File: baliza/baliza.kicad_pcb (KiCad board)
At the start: 2 copper layers, 76.2 x 66 mm, 27 parts, among them J1 ALIMENTACION, J2 PTT, J3 AUDIO, J4 VCC_13v8_ENTRADA, K1 SRD-05VDC-SL-C, K2 SRD-05VDC-SL-C, Q1 2N3904, Q2 2N3904, U1 L7805

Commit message: actualizacion
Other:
- board text added: "+5V OUT"
- board text added: "13v8 ENTRADA"
- board text added: "7805"
- board text added: "ALIMENTACION"
- board text added: "APAGADO 1"
- board text added: "APAGADO 2"
- board text added: "APAGADO 3"
- board text added: "AUDIO"
- board text added: "GND"
- board text added: "PTT"
- board text added: "RESET"
- board text added: "VCC INPUT"
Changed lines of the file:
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@@
     (property "Sheetname" "")
     (attr through_hole)
-    (fp_text reference "K1" (at 8.1 9.2) (layer "F.SilkS")
+    (fp_text reference "K1" (at 14.4 -8.89) (layer "F.SilkS")
       (effects (font (size 1 1) (thickness 0.15)))
     )
@@
     (property "Sheetname" "")
     (attr through_hole)
-    (fp_text reference "C2" (at 2.5 -2.5) (layer "F.SilkS")
+    (fp_text reference "C2" (at 7.58 0) (layer "F.SilkS")
       (effects (font (size 1 1) (thickness 0.15)))
     )
@@
     (property "Sheetname" "")
     (attr through_hole)
-    (fp_text reference "D1" (at 5.08 -2.47 90) (layer "F.SilkS")
+    (fp_text reference "D1" (at -2.54 0 90) (layer "F.SilkS")
       (effects (font (size 1 1) (thickness 0.15)))
     )
@@
     (property "Sheetname" "")
     (attr through_hole)
-    (fp_text reference "D2" (at 5.08 -2.47 90) (layer "F.SilkS")
+    (fp_text reference "D2" (at -2.54 0 90) (layer "F.SilkS")
       (effects (font (size 1 1) (thickness 0.15)))
     )
@@
     (property "Sheetname" "")
     (attr through_hole)
-    (fp_text reference "J1" (at 2.5 -6.06) (layer "F.SilkS")
+    (fp_text reference "J1" (at -5.08 3.175) (layer "F.SilkS")
       (effects (font (size 1 1) (thickness 0.15)))
     )
@@
     (property "Sheetname" "")
     (attr exclude_from_pos_files)
-    (fp_text reference "JP4" (at 0 -1.8 90) (layer "F.SilkS")
+    (fp_text reference "JP4" (at 0 -3.175 180) (layer "F.SilkS")
       (effects (font (size 1 1) (thickness 0.15)))
     )
@@
   (gr_line (start 88.9 53.34) (end 162.56 53.34) (layer "Edge.Cuts") (width 0.1))
   (gr_line (start 165.1 119.38) (end 88.9 119.38) (layer "Edge.Cuts") (width 0.1))
+  (gr_text "VCC INPUT" (at 133.35 58.42 90) (layer "F.SilkS")
+    (effects (font (size 1 1) (thickness 0.15)))
+  )
+  (gr_text "GND" (at 138.43 115.57) (layer "F.SilkS")
+    (effects (font (size 1 1) (thickness 0.15)))
+  )
+  (gr_text "13v8 ENTRADA" (at 99.06 66.675) (layer "F.SilkS")
+    (effects (font (size 1 1) (thickness 0.15)))
+  )
+  (gr_text "GND" (at 106.68 58.42 90) (layer "F.SilkS")
+    (effects (font (size 1 1) (thickness 0.15)))
+  )
+  (gr_text "PTT" (at 100.33 107.315) (layer "F.SilkS")
+    (effects (font (size 1 1) (thickness 0.15)))
+  )
   (gr_text "BALIZA EA7HG-F4LEC" (at 162.56 93.98 90) (layer "F.SilkS")
     (effects (font (size 2 2) (thickness 0.15)))
   )
+  (gr_text "APAGADO 2" (at 129.54 104.14 90) (layer "F.SilkS")
+    (effects (font (size 1 1) (thickness 0.15)))
+  )
+  (gr_text "RESET" (at 133.35 72.39) (layer "F.SilkS")
+    (effects (font (size 1 1) (thickness 0.15)))
+  )
+  (gr_text "VCC INPUT" (at 114.3 63.5 90) (layer "F.SilkS")
+    (effects (font (size 1 1) (thickness 0.15)))
+  )
+  (gr_text "7805" (at 120.65 58.42) (layer "F.SilkS")
+    (effects (font (size 1 1) (thickness 0.15)))
+  )
+  (gr_text "+5V OUT" (at 127 64.135 90) (layer "F.SilkS")
+    (effects (font (size 1 1) (thickness 0.15)))
+  )
+  (gr_text "ALIMENTACION\n" (at 139.7 64.77) (layer "F.SilkS")
+    (effects (font (size 1 1) (thickness 0.15)))
+  )
+  (gr_text "GND" (at 105.41 108.585) (layer "F.SilkS")
+    (effects (font (size 1 1) (thickness 0.15)))
+  )
+  (gr_text "AUDIO" (at 111.76 107.315) (layer "F.SilkS")
+    (effects (font (size 1 1) (thickness 0.15)))
+  )
+  (gr_text "APAGADO 1" (at 124.46 104.14 90) (layer "F.SilkS")
+    (effects (font (size 1 1) (thickness 0.15)))
+  )
+  (gr_text "APAGADO  3" (at 134.62 104.14 90) (layer "F.SilkS")
+    (effects (font (size 1 1) (thickness 0.15)))
+  )
+  (gr_text "GND" (at 146.05 58.42 90) (layer "F.SilkS")
+    (effects (font (size 1 1) (thickness 0.15)))
+  )
   (segment (start 139.7 74.93) (end 133.35 74.93) (width 1) (layer "F.Cu") (net 3))

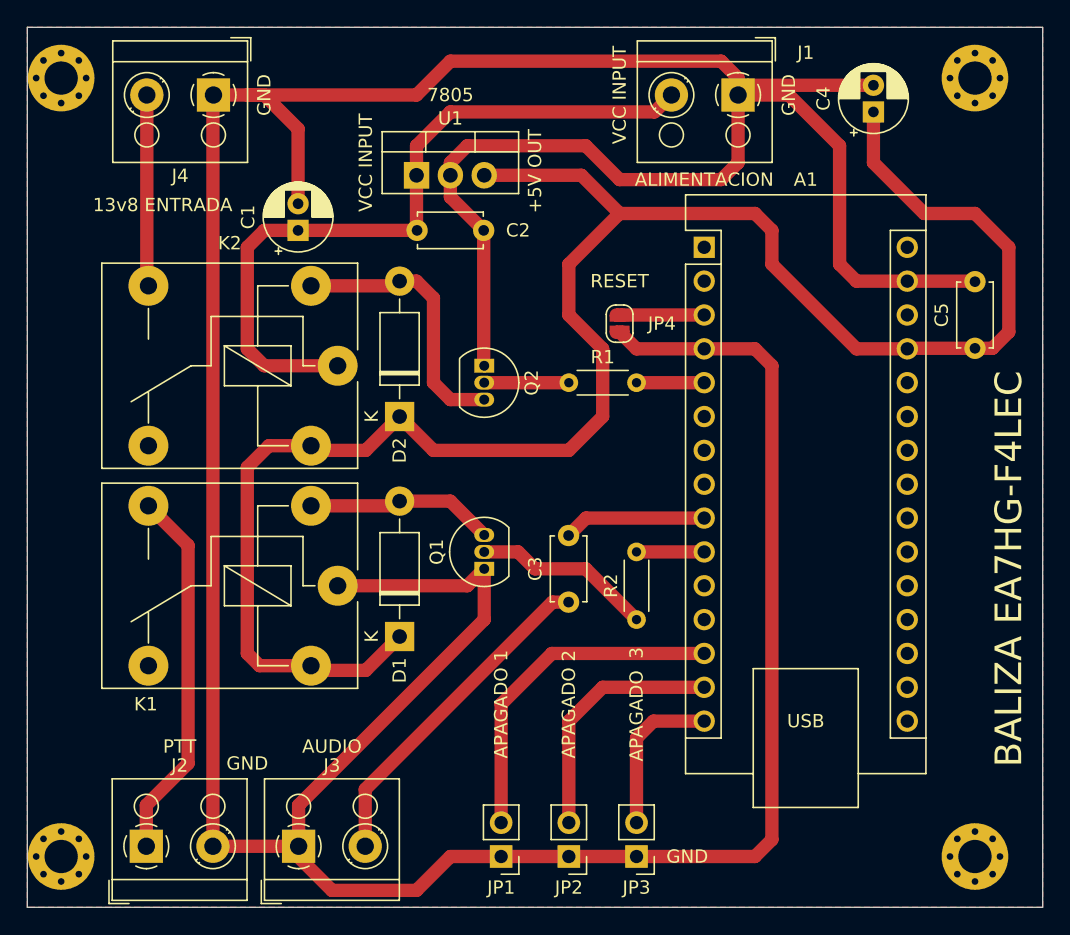
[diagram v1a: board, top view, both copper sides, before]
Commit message: anadir LEDs auxiliares, pistas en cara inferior
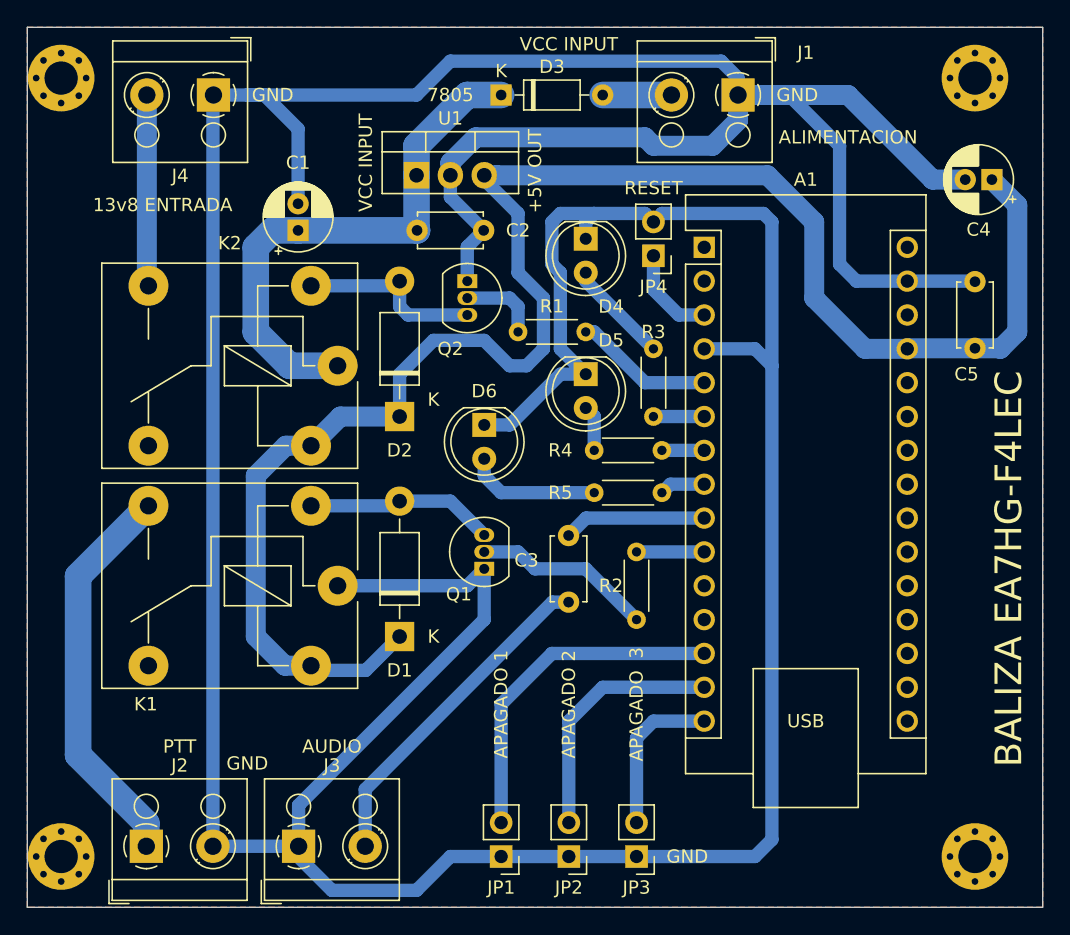
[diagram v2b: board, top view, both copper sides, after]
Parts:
- added D3: 1N4148, Diode_THT:D_DO-35_SOD27_P7.62mm_Horizontal, F.Cu at (124.5, 58.4)
- added D4: LED, LED_THT:LED_D5.0mm, F.Cu at (130.8, 69.2)
- added D5: LED, LED_THT:LED_D5.0mm, F.Cu at (130.8, 79.4)
- added D6: LED, LED_THT:LED_D5.0mm, F.Cu at (123.2, 83.2)
- added R3: 680, Resistor_THT:R_Axial_DIN0204_L3.6mm_D1.6mm_P5.08mm_Horizontal, F.Cu at (135.9, 82.5)
- added R4: 680, Resistor_THT:R_Axial_DIN0204_L3.6mm_D1.6mm_P5.08mm_Horizontal, F.Cu at (136.5, 85.1)
- added R5: 680, Resistor_THT:R_Axial_DIN0204_L3.6mm_D1.6mm_P5.08mm_Horizontal, F.Cu at (136.5, 88.3)
- JP4: footprint Jumper:SolderJumper-2_P1.3mm_Open_RoundedPad1.0x1.5mm -> Connector_PinHeader_2.54mm:PinHeader_1x02_P2.54mm_Vertical
- moved C4 10.2 mm to (161.3, 64.8), turned to 180 degrees
- moved Q2 6.48 mm to (121.9, 72.4)
- moved JP4 5.69 mm to (135.9, 70.5), turned to 180 degrees
- moved R1 5.39 mm to (125.7, 76.2)
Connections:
- A1 pad 6: unconnected-(A1-Pad6) -> AUX1
- A1 pad 7: unconnected-(A1-Pad7) -> AUX2
- A1 pad 8: unconnected-(A1-Pad8) -> AUX3
- J1 pad 2: VCC -> +BATT
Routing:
- net GND: track 324.9 -> 371.2 mm
- net VCC: track 55.3 -> 40.5 mm
- net +5V: track 145.2 -> 130.8 mm
- net Net-(D6-Pad2): track 0.00 -> 10.1 mm
- net Net-(D4-Pad2): track 0.00 -> 7.82 mm
- net Net-(D2-Pad2): track 20.5 -> 14.0 mm
- net /Rele encendido: track 5.08 -> 10.5 mm
- net +BATT: track 0.00 -> 5.16 mm
- net AUX1: track 0.00 -> 3.81 mm
- net Net-(D5-Pad2): track 0.00 -> 3.44 mm
- net AUX3: track 0.00 -> 3.44 mm
- net AUX2: track 0.00 -> 3.17 mm
- net PTT_TRANSCEPTOR: track 28.1 -> 29.9 mm
- net Net-(A1-Pad3): track 6.35 -> 7.14 mm
- added copper zone on B.Cu, net GND
